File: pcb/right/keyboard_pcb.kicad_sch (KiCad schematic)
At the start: 33 parts, among them J1 TRRS, K00 KEYSW, K01 KEYSW, K02 KEYSW, K03 KEYSW, K04 KEYSW, K05 KEYSW, K10 KEYSW, K11 KEYSW, K12 KEYSW, K13 KEYSW, K14 KEYSW, K15 KEYSW, K20 KEYSW, K21 KEYSW, K22 KEYSW, K23 KEYSW, K24 KEYSW, K25 KEYSW, K30 KEYSW, K31 KEYSW, K32 KEYSW, U2 Pico

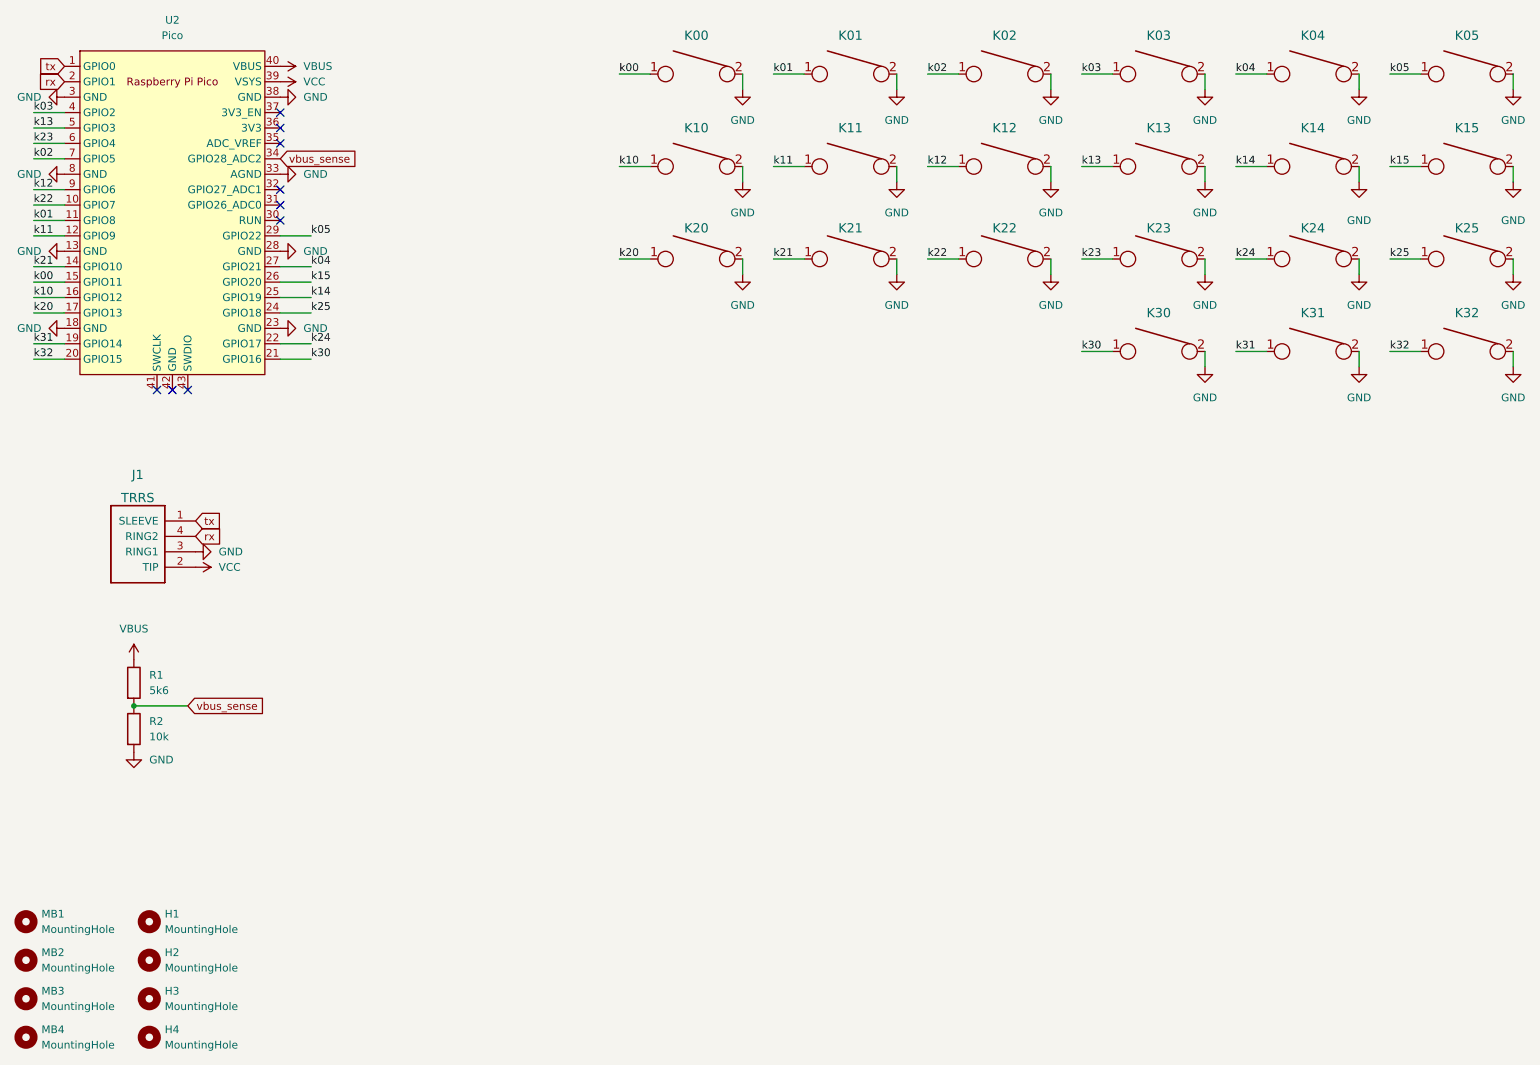
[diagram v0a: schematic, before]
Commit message: Switched to 0xCB Helios controller
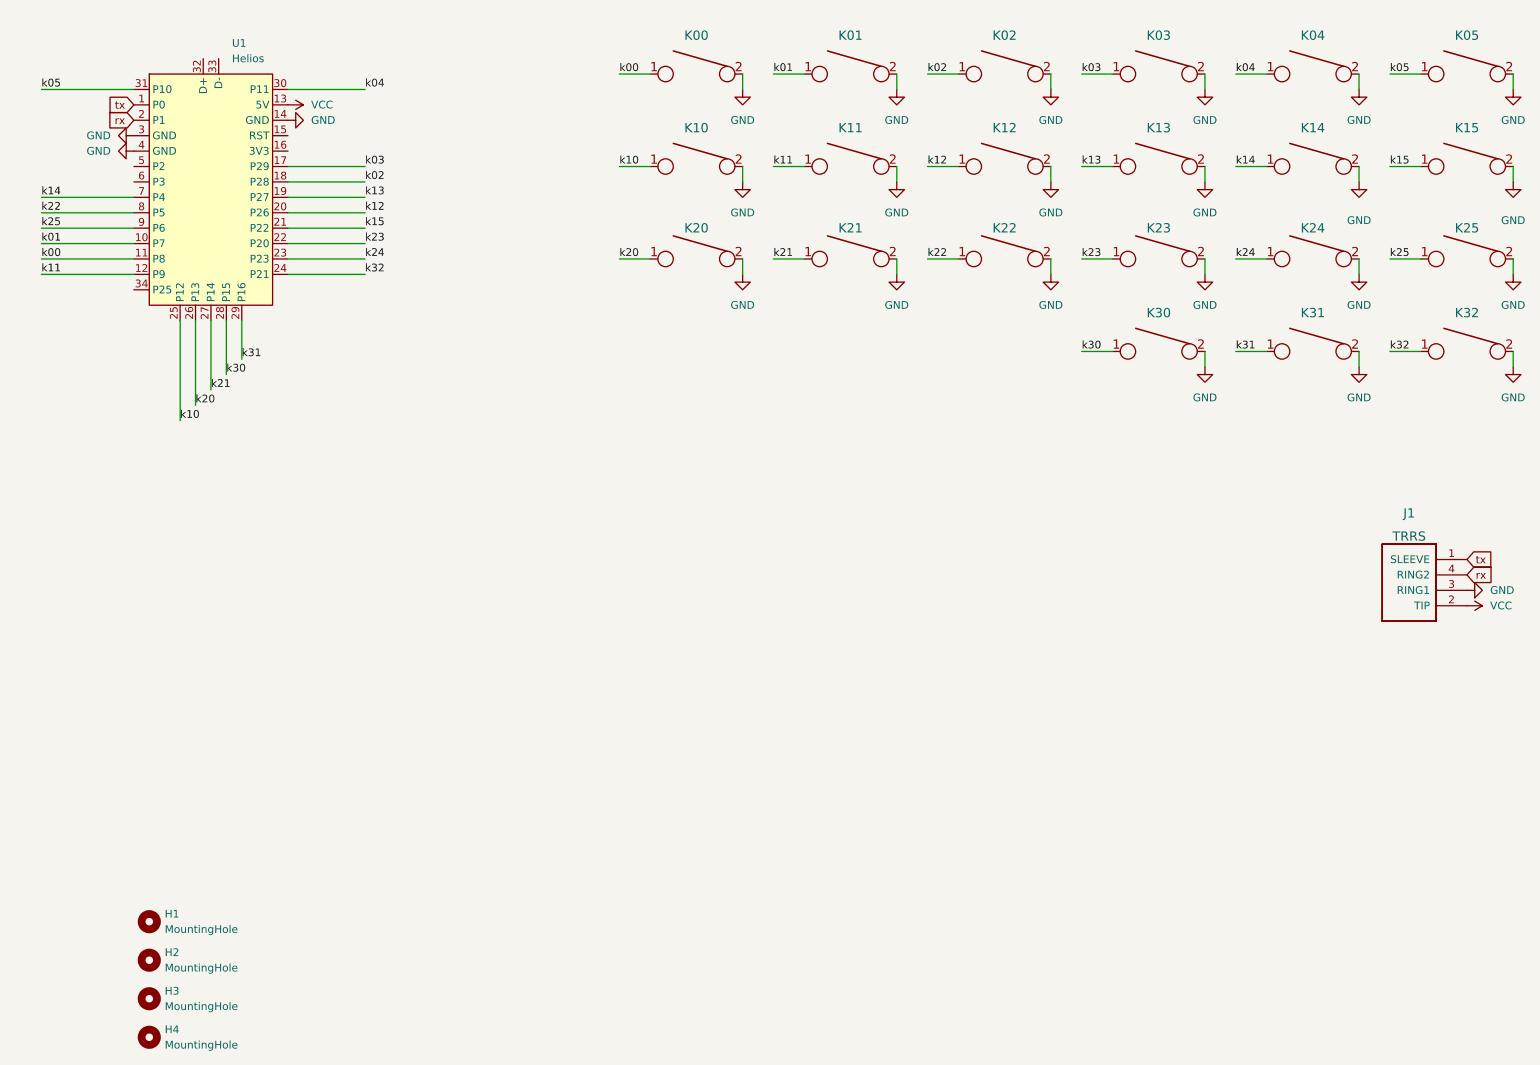
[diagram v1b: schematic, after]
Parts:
- removed MB1, MB2, MB3, MB4: MountingHole, beekeeb_lib:mousebites, symbol Mechanical:MountingHole
- removed R1: 5k6, Resistor_SMD:R_1206_3216Metric_Pad1.30x1.75mm_HandSolder, symbol Device:R
- removed R2: 10k, Resistor_SMD:R_1206_3216Metric_Pad1.30x1.75mm_HandSolder, symbol Device:R
- removed U2: Pico, RPi_Pico:RPi_Pico_SMD_TH, symbol KiCad-RP-Pico:Pico
- added U1: Helios, PCM_marbastlib-xp-promicroish:Helios_AH_USBdn, symbol PCM_marbastlib-promicroish:Helios
- J1: footprint Resistor_SMD:R_1206_3216Metric_Pad1.30x1.75mm_HandSolder -> Keebio-Parts:TRRS-PJ-320A
- K00, K01, K02, K03, K04, K05, K10, K11, K12, K13, K14, K15, K20, K21, K22, K23, K24, K25, K30, K31, K32: footprint keyswitches:SW_PG1350_reversible -> keyswitches:Kailh_socket_PG1350_optional
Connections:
- net GND: now also U1.14 (GND), U1.3 (GND), U1.4 (GND)
- net VCC: now also U1.13 (5V)
- net k00: now also U1.11 (P8)
- net k01: now also U1.10 (P7)
- net k02: now also U1.18 (P28)
- net k03: now also U1.17 (P29)
- net k04: now also U1.30 (P11)
- net k05: now also U1.31 (P10)
- net k10: now also U1.25 (P12)
- net k11: now also U1.12 (P9)
- net k12: now also U1.20 (P26)
- net k13: now also U1.19 (P27)
- net k14: now also U1.7 (P4)
- net k15: now also U1.21 (P22)
- net k20: now also U1.26 (P13)
- net k21: now also U1.27 (P14)
- net k22: now also U1.8 (P5)
- net k23: now also U1.22 (P20)
- net k24: now also U1.23 (P23)
- net k25: now also U1.9 (P6)
- net k30: now also U1.28 (P15)
- net k31: now also U1.29 (P16)
- net k32: now also U1.24 (P21)
- net rx: now also U1.2 (P1)
- net tx: now also U1.1 (P0)
- no-connect marks 9 -> 0
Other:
- moved on the sheet: J1

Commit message: Add ground plane. Add reset pins.
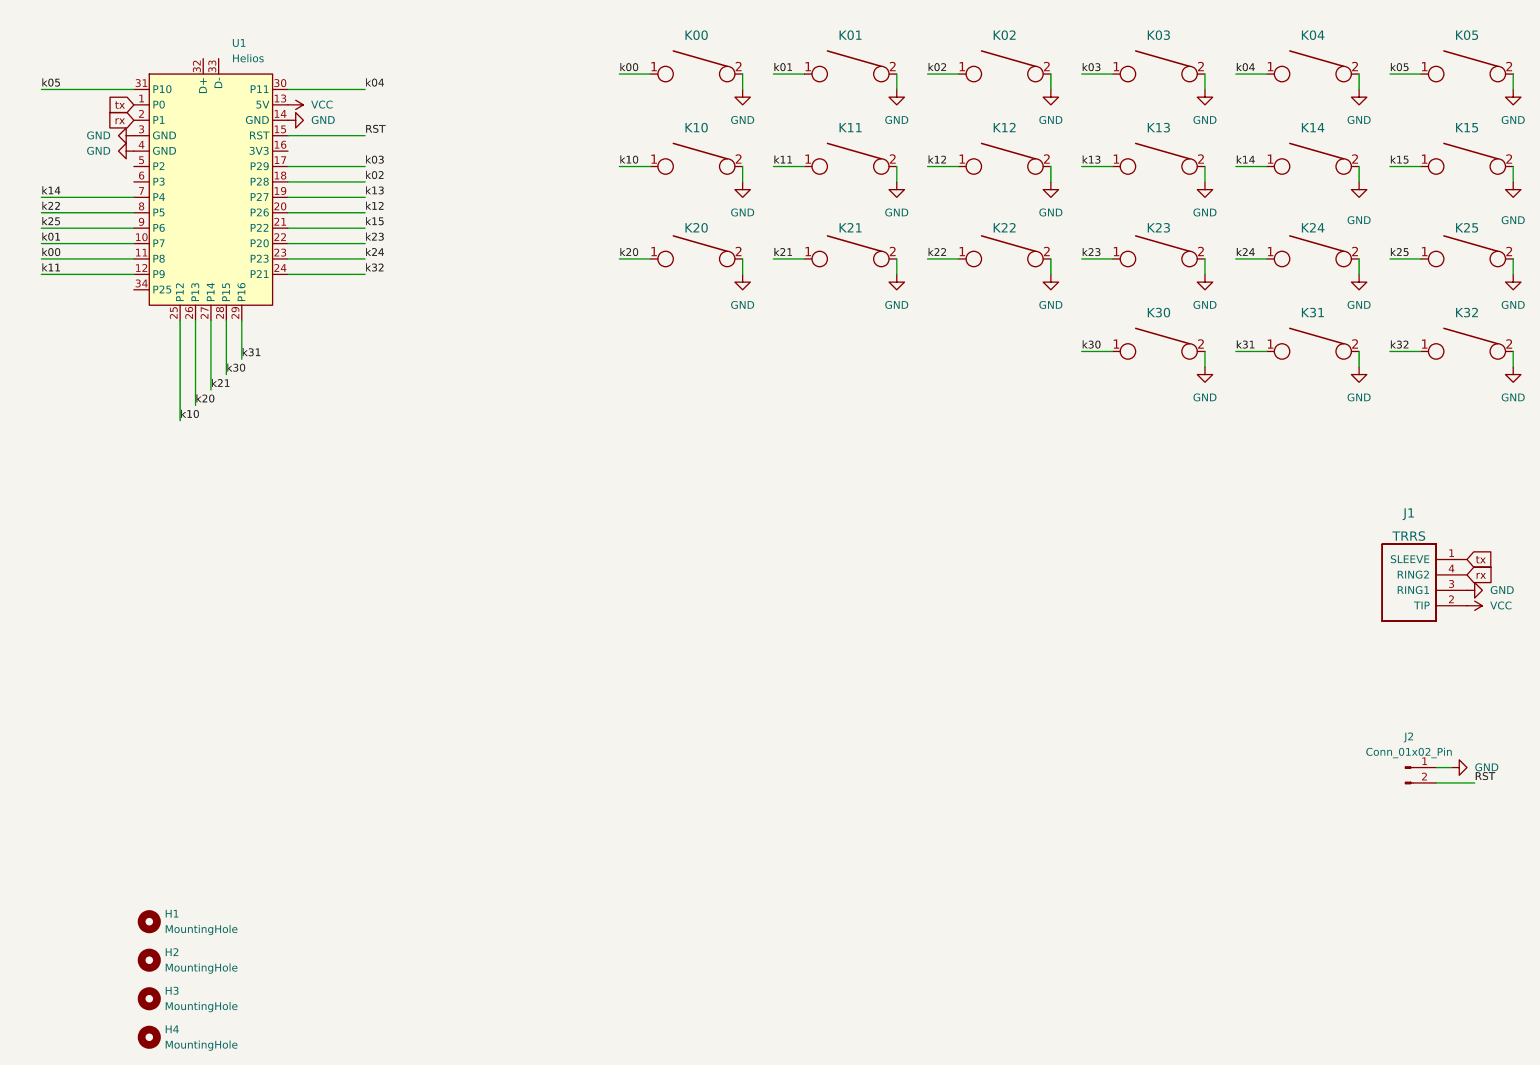
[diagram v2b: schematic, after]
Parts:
- added J2: Conn_01x02_Pin, Connector_PinHeader_2.54mm:PinHeader_1x02_P2.54mm_Vertical, symbol Connector:Conn_01x02_Pin
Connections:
- net GND: now also J2.1 (Pin_1)
- net RST: now reaches U1.15 (RST)
- net RST: now also J2.2 (Pin_2)
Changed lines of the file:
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@@
+	(wire
+		(pts
+			(xy 259.08 144.78) (xy 261.62 144.78)
+		)
+		(stroke
+			(width 0)
+			(type default)
+		)
+	)
 	(wire
 		(pts
@@
 	(wire
 		(pts
+			(xy 259.08 147.32) (xy 265.43 147.32)
+		)
+		(stroke
+			(width 0)
+			(type default)
+		)
+	)
+	(wire
+		(pts
 			(xy 175.26 30.48) (xy 180.34 30.48)
 		)
@@
 		(pts
 			(xy 69.85 63.5) (xy 82.55 63.5)
+		)
+		(stroke
+			(width 0)
+			(type default)
+		)
+	)
+	(wire
+		(pts
+			(xy 69.85 40.64) (xy 82.55 40.64)
 		)
 		(stroke
@@
 		)
 	)
+	(label "RST"
+		(at 265.43 147.32 0)
+		(fields_autoplaced yes)
+		(effects
+			(font
+				(size 1.27 1.27)
+			)
+			(justify left bottom)
+		)
+	)
 	(label "k02"
 		(at 82.55 48.26 0)
@@
 	(label "k23"
 		(at 200.66 60.96 0)
+		(fields_autoplaced yes)
+		(effects
+			(font
+				(size 1.27 1.27)
+			)
+			(justify left bottom)
+		)
+	)
+	(label "RST"
+		(at 82.55 40.64 0)
 		(fields_autoplaced yes)
 		(effects
@@
 				(path "/9538e4ed-27e6-4c37-b989-9859dc0d49e8"
 					(reference "K32")
+					(unit 1)
+				)
+			)
+		)
+	)
+	(symbol
+		(lib_id "power:GND")
+		(at 261.62 144.78 90)
+		(unit 1)
+		(exclude_from_sim no)
+		(in_bom yes)
+		(on_board yes)
+		(dnp no)
+		(fields_autoplaced yes)
+		(property "Reference" "#PWR02"
+			(at 267.97 144.78 0)
+			(effects
+				(font
+					(size 1.27 1.27)
+				)
+				(hide yes)
+			)
+		)
+		(property "Value" "GND"
+			(at 265.43 144.7799 90)
+			(effects
+				(font
+					(size 1.27 1.27)
+				)
+				(justify right)
+			)
+		)
+		(property "Footprint" ""
+			(at 261.62 144.78 0)
+			(effects
+				(font
+					(size 1.27 1.27)
+				)
+				(hide yes)
+			)
+		)
+		(property "Datasheet" ""
+			(at 261.62 144.78 0)
+			(effects
+				(font
+					(size 1.27 1.27)
+				)
+				(hide yes)
+			)
+		)
+		(property "Description" ""
+			(at 261.62 144.78 0)
+			(effects
+				(font
+					(size 1.27 1.27)
+				)
+				(hide yes)
+			)
+		)
+		(pin "1"
+		)
+		(instances
+			(project "keyboard_pcb"
+				(path "/9538e4ed-27e6-4c37-b989-9859dc0d49e8"
+					(reference "#PWR02")
 					(unit 1)
 				)
@@
 					(unit 1)
 				)
+			)
+		)
+	)
+	(symbol
+		(lib_id "Connector:Conn_01x02_Pin")
+		(at 254 144.78 0)
+		(unit 1)
+		(exclude_from_sim no)
+		(in_bom yes)
+		(on_board yes)
+		(dnp no)
+		(fields_autoplaced yes)
+		(property "Reference" "J2"
+			(at 254.635 139.7 0)
+			(effects
+				(font
+					(size 1.27 1.27)
+				)
+			)
+		)
+		(property "Value" "Conn_01x02_Pin"
+			(at 254.635 142.24 0)
+			(effects
+				(font
+					(size 1.27 1.27)
+				)
+			)
+		)
+		(property "Footprint" "Connector_PinHeader_2.54mm:PinHeader_1x02_P2.54mm_Vertical"
+			(at 254 144.78 0)
+			(effects
+				(font
+					(size 1.27 1.27)
+				)
+				(hide yes)
+			)
+		)
+		(property "Datasheet" "~"
+			(at 254 144.78 0)
+			(effects
+				(font
+					(size 1.27 1.27)
+				)
+				(hide yes)
+			)
+		)
+		(property "Description" "Generic connector, single row, 01x02, script generated"
+			(at 254 144.78 0)
+			(effects
+				(font
+					(size 1.27 1.27)
+				)
+				(hide yes)
+			)
+		)
+		(pin "2"
+		)
+		(pin "1"
+		)
+		(instances
+			(project ""
+				(path "/9538e4ed-27e6-4c37-b989-9859dc0d49e8"
+					(reference "J2")
+					(unit 1)
+				)

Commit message: Rotate TRRS jack. Replace reset pins by reset button.
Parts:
- J2: footprint Connector_PinHeader_2.54mm:PinHeader_1x02_P2.54mm_Vertical -> PCM_marbastlib-various:SW_SKHLLCA010
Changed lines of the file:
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@@
 			)
 		)
-		(property "Footprint" "Connector_PinHeader_2.54mm:PinHeader_1x02_P2.54mm_Vertical"
+		(property "Footprint" "PCM_marbastlib-various:SW_SKHLLCA010"
 			(at 254 144.78 0)
 			(effects
